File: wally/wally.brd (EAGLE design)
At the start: 41 x 101 mm, 103 parts, among them IC1 ESP32-S3-WROOM-1U-N16, IC2 XTLV61048DBVR, IC3 TLV1117LV33DCYR, IC4 DPS310XTSA1, IC5 BMI323, IC6 MCP96L00T-E_MX, IC7 MLX90395KLW-BBA-001-SP, J1 MSD-4-A, J2 QWIIC_RIGHT_ANGLE, J3 QWIIC_RIGHT_ANGLE, J4 S2B-PH-K-S(LF)(SN), J5 USB4105-GF-A, U1 RA-01H

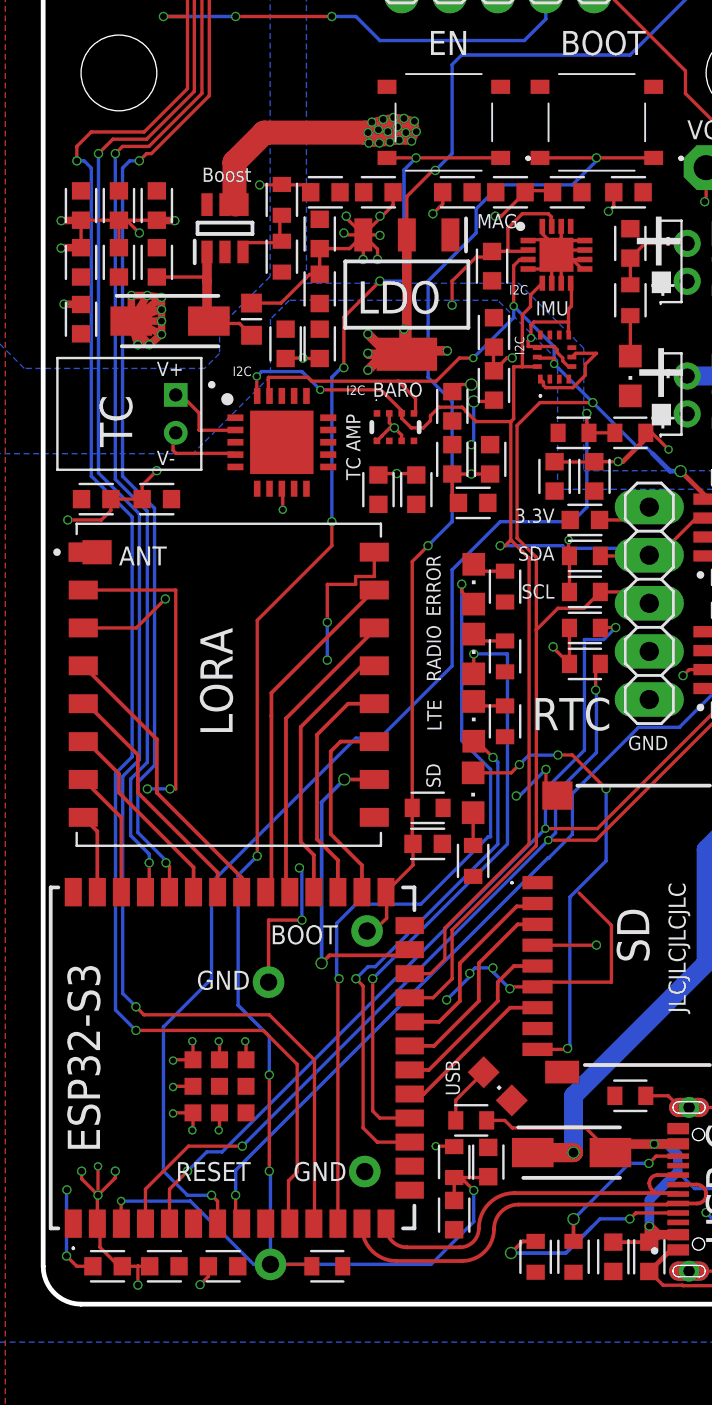
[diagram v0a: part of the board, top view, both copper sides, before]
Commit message: add two generic inputs to wally
had two gpio left lol
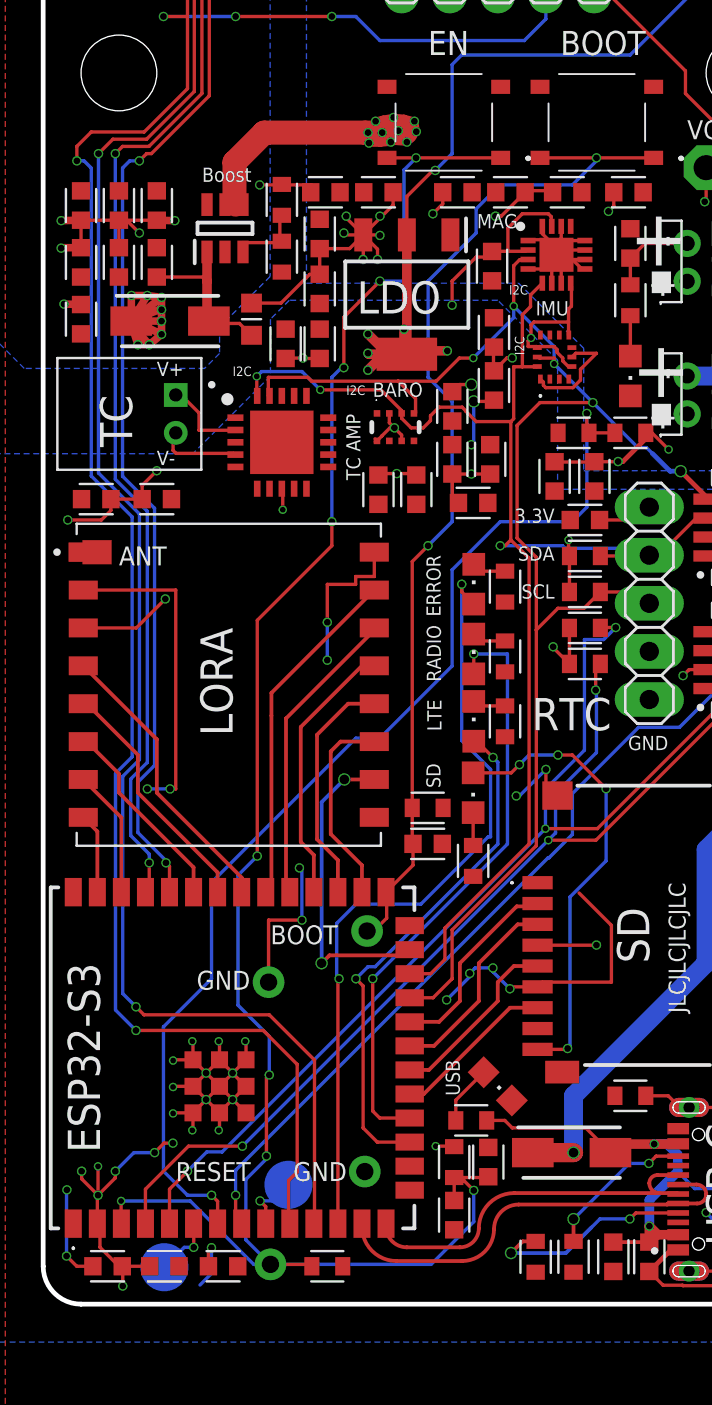
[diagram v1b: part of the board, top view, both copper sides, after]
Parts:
- added TP14, TP15: PTR1B2,54, testpad:B2,54
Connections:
- new net A0: IC1.6, TP15.TP
- new net A1: IC1.9, TP14.TP
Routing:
- net GND: track 107.3 -> 123.2 mm, vias 27 -> 31
- net 3V3: track 165.1 -> 170.9 mm, vias 30 -> 32
- net A0: track 0.00 -> 3.24 mm, vias 0 -> 1
- net A1: track 0.00 -> 3.18 mm, vias 0 -> 1
- net EN: track 100.2 -> 101.2 mm
- net VCC: track 162.2 -> 161.7 mm, vias 32 -> 26
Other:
- board text added: "A0"
- board text added: "A1"

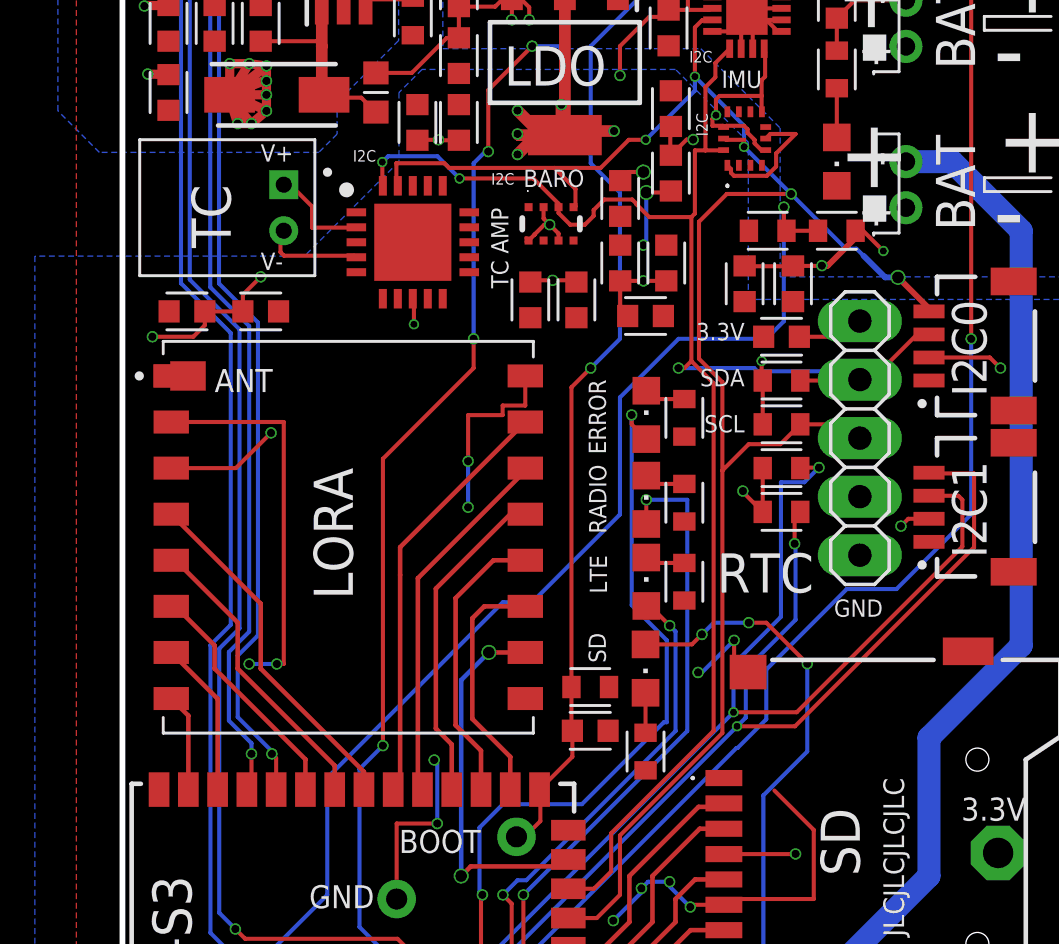
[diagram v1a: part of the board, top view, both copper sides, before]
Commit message: remove thermocouple amp
makes more sense to have it externally and connected through i2c
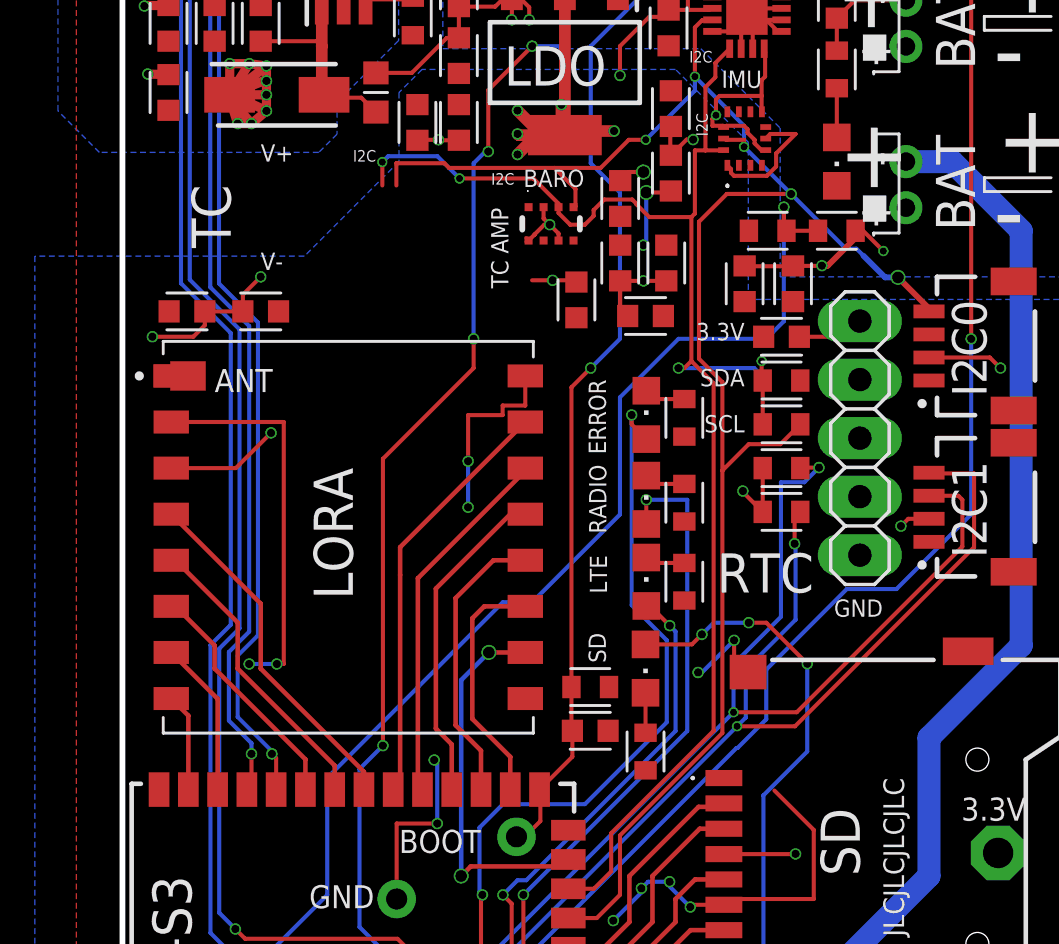
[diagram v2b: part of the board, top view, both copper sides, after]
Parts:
- removed C25: 470n, Capacitor:CAPC1608X85
- removed IC6: MCP96L00T-E_MX, SamacSys_Parts:QFN65P500X500X100-21N
- removed J4: S2B-PH-K-S(LF)(SN), Connectors:S2B-PH-K-S(LF)(SN)
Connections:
- removed net N$5: IC6.4, J4.2
- removed net N$6: IC6.2, J4.1
- net 3V3: no longer C25.2, IC6.8
- net GND: no longer C25.1, IC6.1, IC6.10, IC6.13, IC6.16, IC6.17, IC6.18, IC6.21, IC6.3, IC6.5, IC6.6, IC6.7, IC6.9
- net SCL0: no longer IC6.19, JP1.3
- net SCL1: now also JP1.3
- net SDA0: no longer IC6.20, JP1.4
- net SDA1: now also JP1.4
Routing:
- net SDA0: track 74.2 -> 63.5 mm
- net N$6: track 4.47 -> 0.00 mm
- net N$5: track 4.43 -> 0.00 mm
- net SCL0: track 83.1 -> 80.2 mm
- net 3V3: track 170.9 -> 169.4 mm, vias 32 -> 31

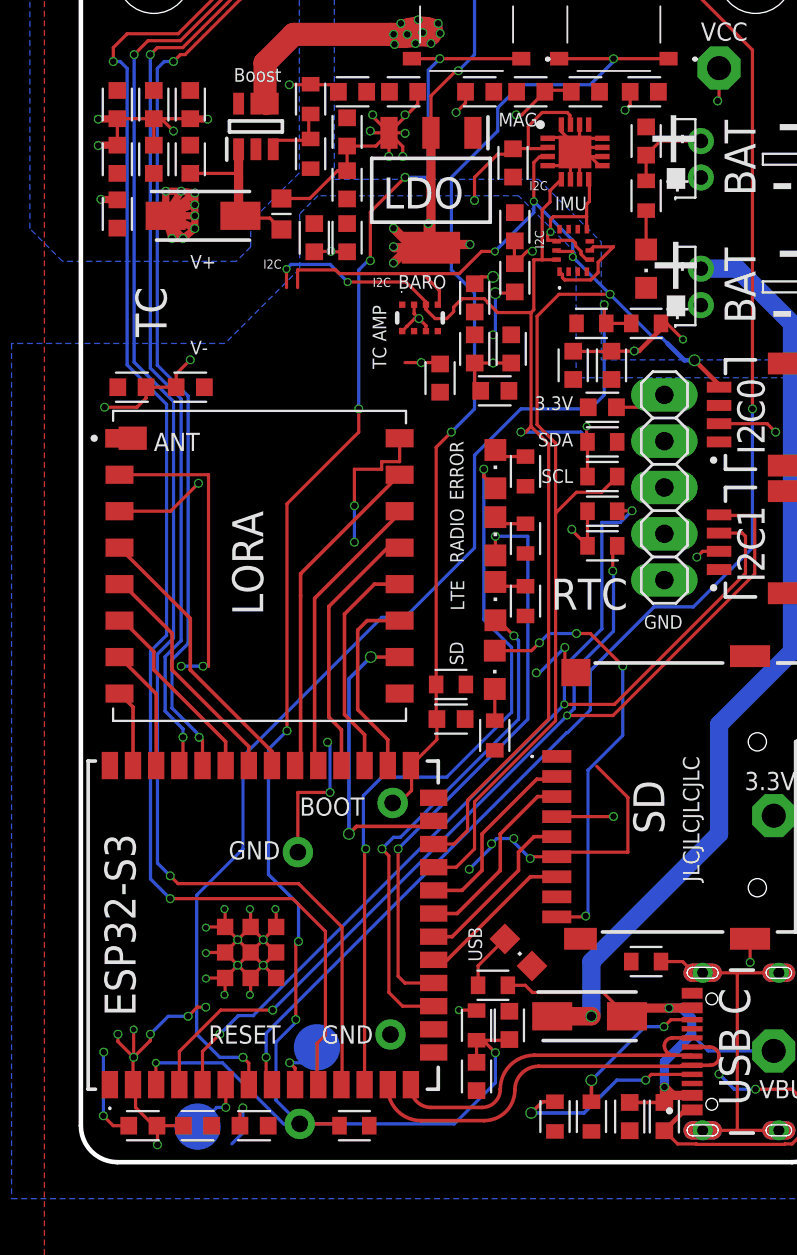
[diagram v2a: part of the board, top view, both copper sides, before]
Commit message: use smaller components where available
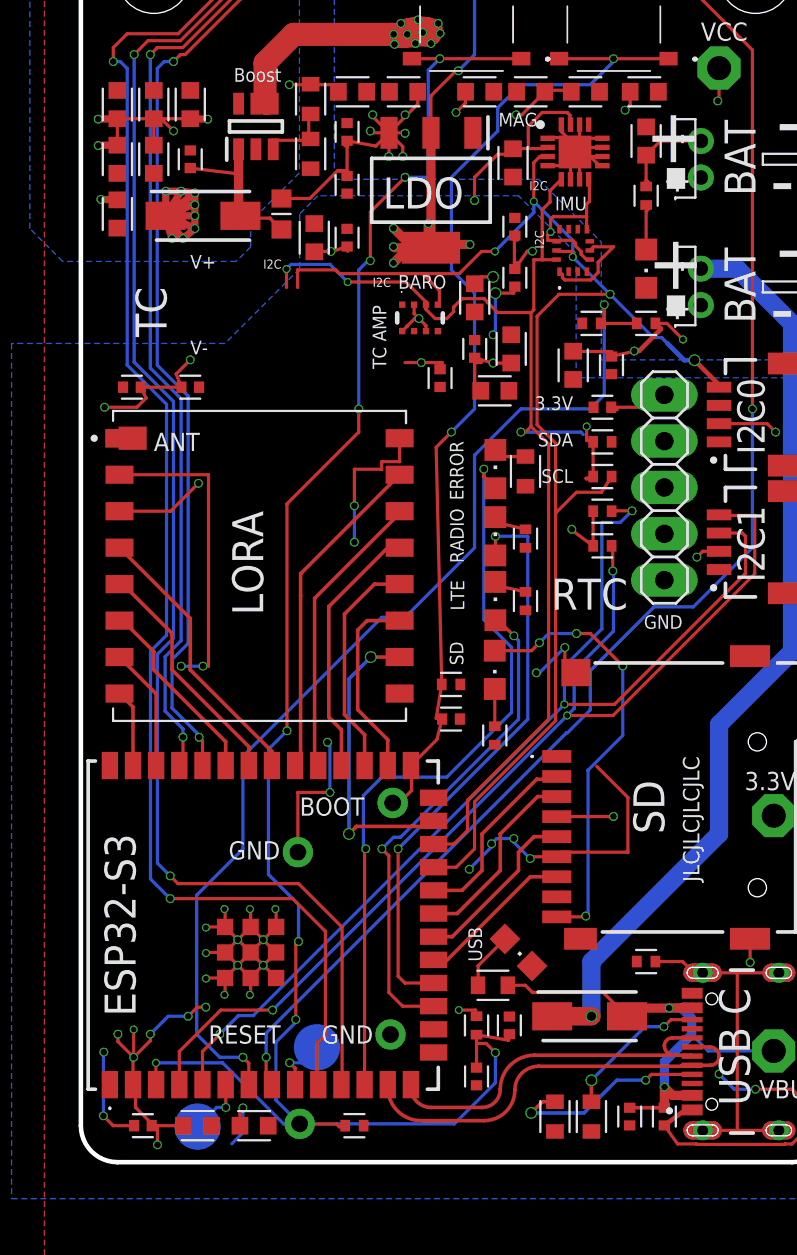
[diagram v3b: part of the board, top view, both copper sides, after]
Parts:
- C1, C10, C11, C13, C14, C15, C16, C17, C19, C23, C26, C27, C28, C29, C3, C35, C8, C9: device Capacitor:CAPC1608X85 -> Capacitor:CAPC1005X60
- R1, R10, R11, R13, R15, R16, R18, R19, R4, R5, R6, R7, R8, R9: device Resistor:RESC1608X60 -> Resistor:RESC1005X40
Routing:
- net 3V3: track 169.4 -> 175.3 mm
- net VCC: track 161.7 -> 164.1 mm
- net EN: track 101.2 -> 102.4 mm
- net VSENSE: track 59.4 -> 60.1 mm
- net GND: track 123.2 -> 123.8 mm

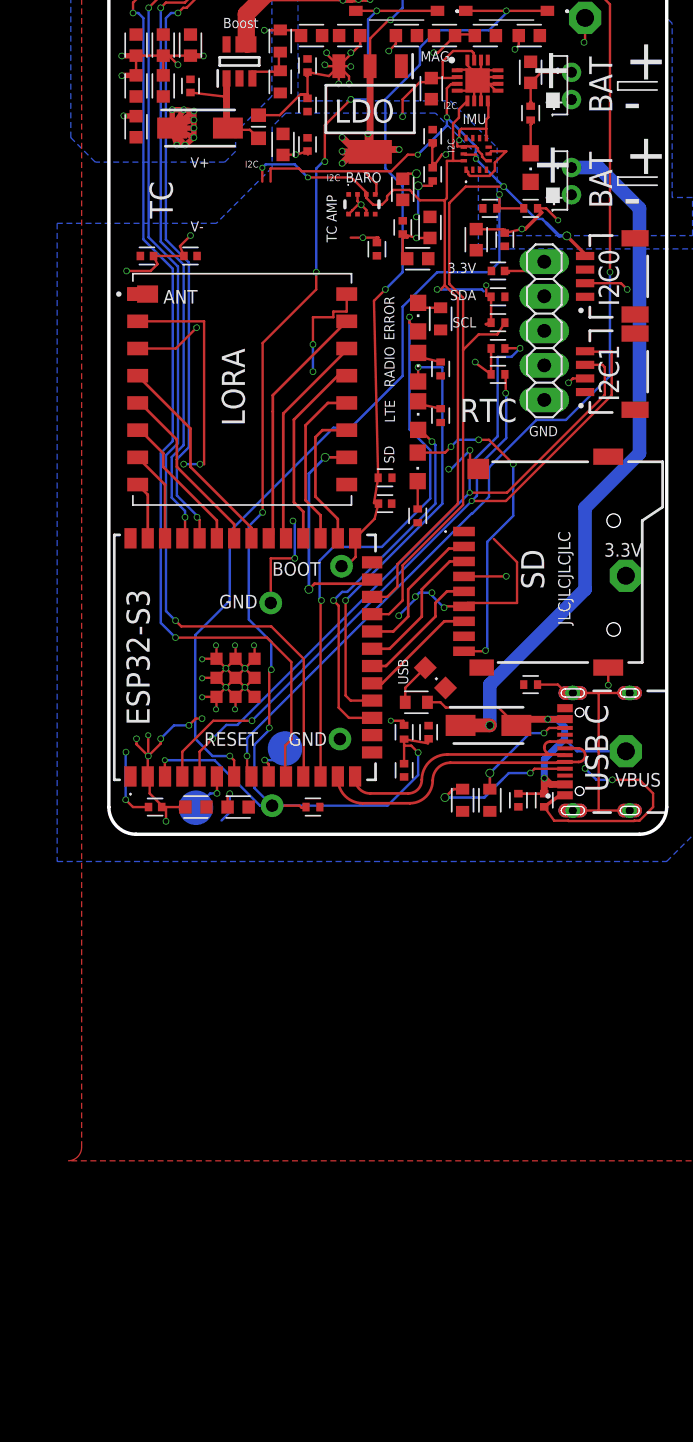
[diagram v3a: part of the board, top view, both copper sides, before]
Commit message: change to lsm6dsv imu
+- 32g and integrated sensor fusion
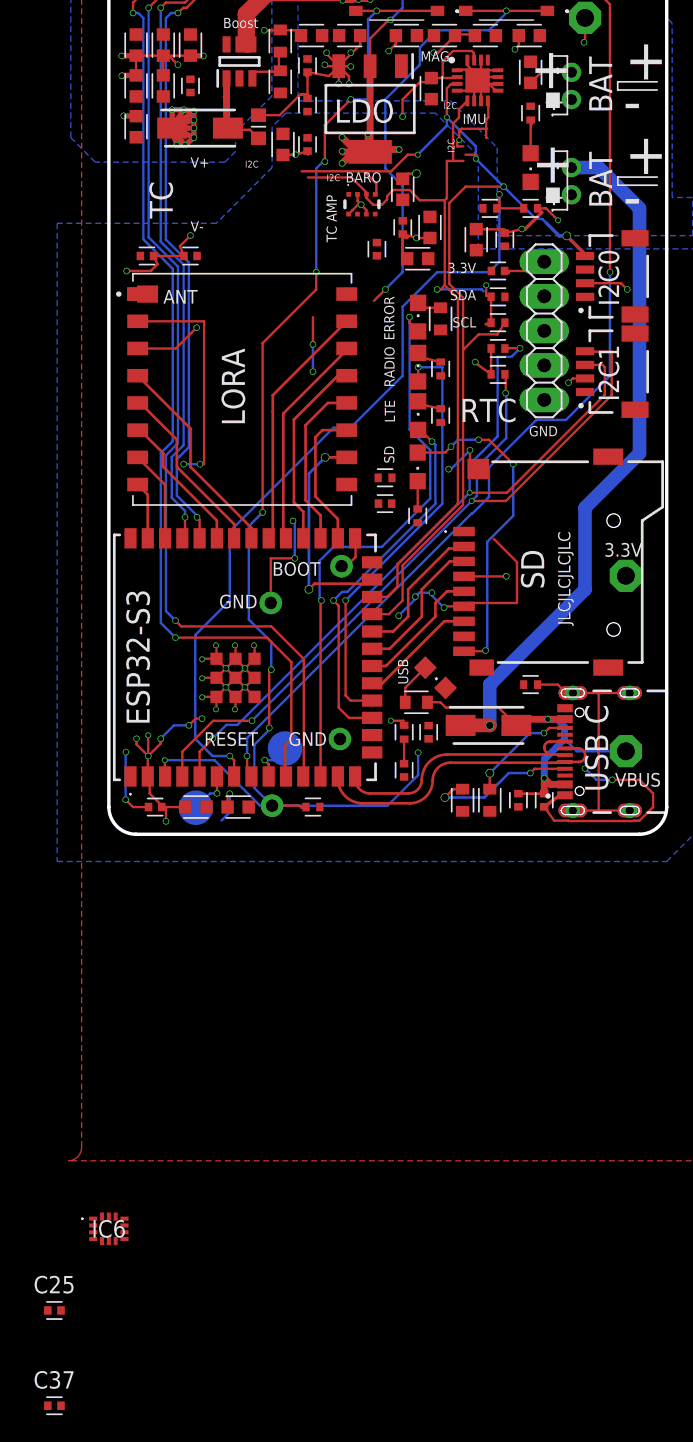
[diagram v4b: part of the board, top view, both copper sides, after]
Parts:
- removed C26, C27: 100n, Capacitor:CAPC1005X60
- removed IC5: BMI323, SamacSys_Parts:BMI323
- added C25, C37: 100n, Capacitor:CAPC1005X60
- added IC6: LSM6DSV16BXTR, SamacSys_Parts:LSM6DSV16BXTR
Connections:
- new net N$5: IC6.14
- new net N$6: IC6.13
- net 3V3: now also C25.1, C37.1, IC6.12, IC6.5, IC6.8; no longer C26.1, C27.1, IC5.12, IC5.5, IC5.8
- net GND: now also C25.2, C37.2, IC6.1, IC6.2, IC6.3, IC6.6, IC6.7; no longer C26.2, C27.2, IC5.1, IC5.6, IC5.7
- net SCL0: no longer IC5.13
- net SDA0: no longer IC5.14
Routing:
- net BOOT: track 55.7 -> 37.3 mm
- net GND: track 123.8 -> 108.9 mm, vias 31 -> 28
- net 3V3: track 175.3 -> 165.4 mm, vias 31 -> 29
- net SDA0: track 63.5 -> 58.6 mm, vias 3 -> 1
- net SCL0: track 80.0 -> 76.5 mm
- net EN: track 102.4 -> 99.0 mm
- net N$2: track 9.34 -> 6.89 mm
- net VCC: track 164.1 -> 162.1 mm
